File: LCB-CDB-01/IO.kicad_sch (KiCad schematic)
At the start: 64 parts, among them J100 Conn_01x02, J101 Conn_01x02, J102 Conn_01x02, J103 Conn_01x02, J104 Conn_01x02, J105 Conn_01x02, J106 Conn_01x02, J107 Conn_01x02, J130 Conn_01x02, J131 Conn_01x02, J132 Conn_01x02, J133 Conn_01x02, J134 Conn_01x02, J135 Conn_01x02, J136 Conn_01x02, J137 Conn_01x02, J138 Conn_01x02, J139 Conn_01x02, J140 Conn_01x02, J141 Conn_01x02, J150 Conn_01x02, J151 Conn_01x02, J152 Conn_01x02, J153 Conn_01x02, J154 Conn_01x02, J155 Conn_01x02, J156 Conn_01x02, J157 Conn_01x02, J158 Conn_01x02, J159 Conn_01x02, J160 Conn_01x02, J161 Conn_01x02, SW1 SW_Push, SW2 SW_Push, SW3 SW_Push, SW4 SW_Push, U100 ST_6CH_CMOS_SOIC14_MC74HC14ADG, U101 ST_6CH_CMOS_SOIC14_MC74HC14ADG

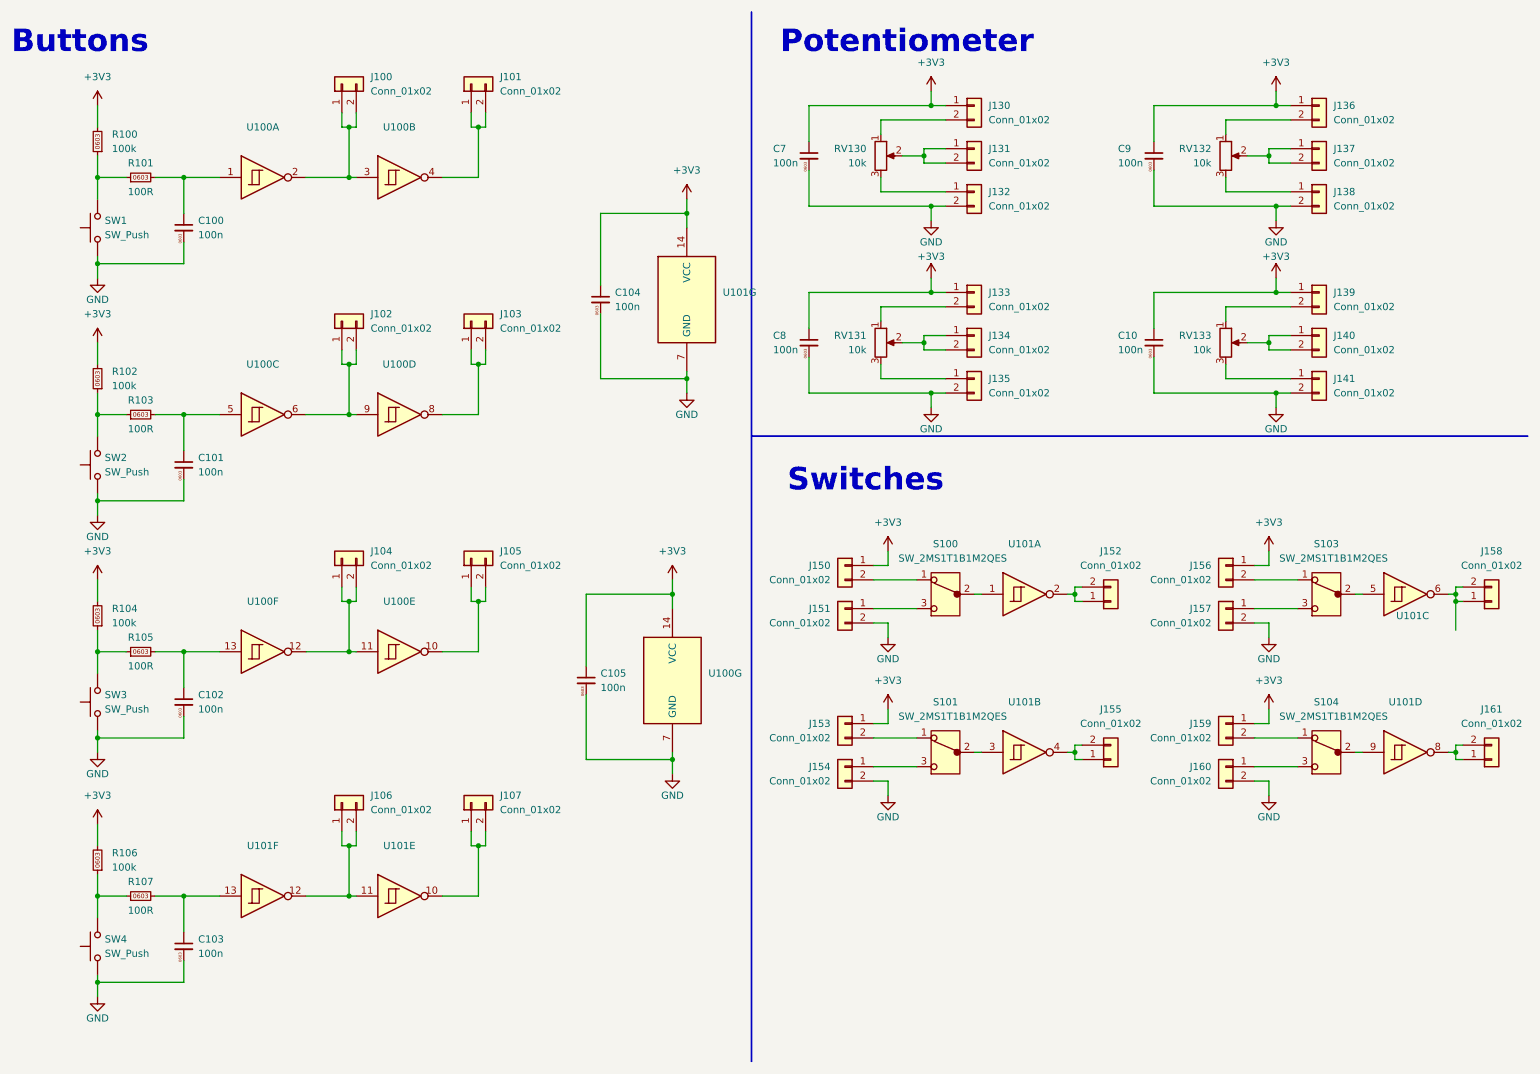
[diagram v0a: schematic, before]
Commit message: update some Rs and Cs names and values, as they can be separate values in KiCad7
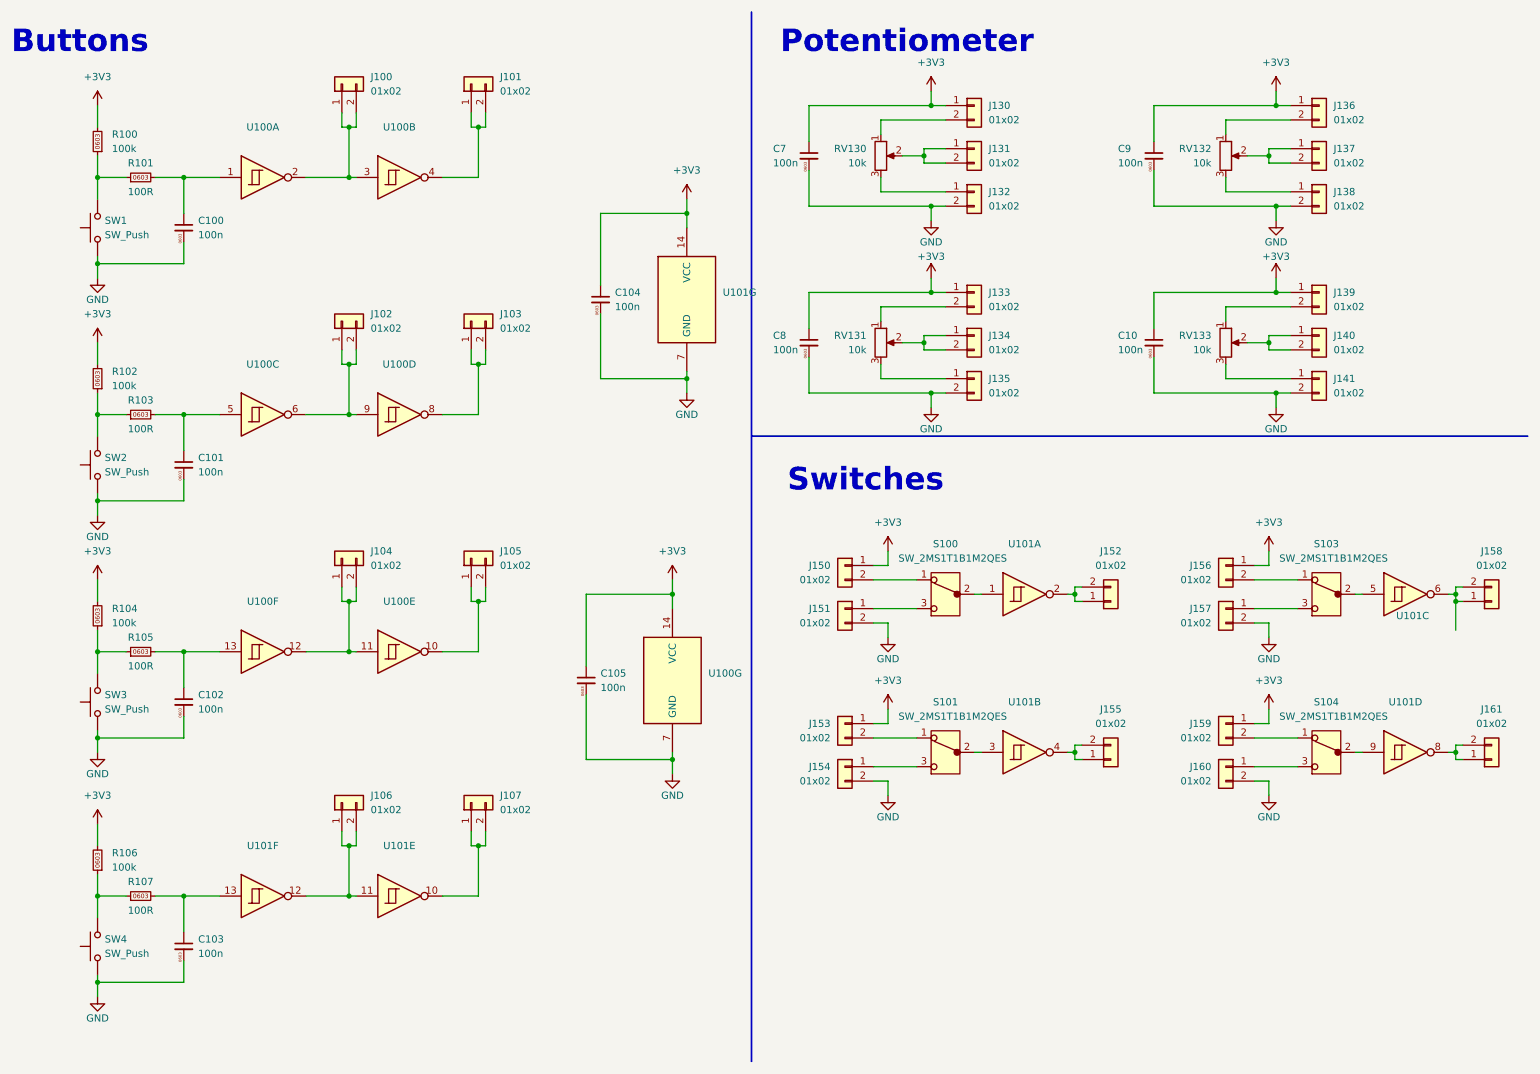
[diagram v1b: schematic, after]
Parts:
- J100, J101, J102, J103, J104, J105, J106, J107, J130, J131, J132, J133, J134, J135, J136, J137, J138, J139, J140, J141, J150, J151, J152, J153, J154, J155, J156, J157, J158, J159, J160, J161: value Conn_01x02 -> 01x02
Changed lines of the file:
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@@
       (effects (font (size 1.27 1.27)) (justify left))
     )
-    (property "Value" "Conn_01x02" (at 189.23 31.7499 0)
+    (property "Value" "01x02" (at 189.23 31.7499 0)
       (effects (font (size 1.27 1.27)) (justify left))
     )
@@
       (effects (font (size 1.27 1.27)) (justify left))
     )
-    (property "Value" "Conn_01x02" (at 161.29 148.5899 0)
+    (property "Value" "01x02" (at 161.29 148.5899 0)
       (effects (font (size 1.27 1.27)) (justify left))
     )
@@
       (effects (font (size 1.27 1.27)) (justify left))
     )
-    (property "Value" "Conn_01x02" (at 228.6 120.6499 0)
+    (property "Value" "01x02" (at 228.6 120.6499 0)
       (effects (font (size 1.27 1.27)) (justify left))
     )
@@
       (effects (font (size 1.27 1.27)) (justify left))
     )
-    (property "Value" "Conn_01x02" (at 189.23 72.3899 0)
+    (property "Value" "01x02" (at 189.23 72.3899 0)
       (effects (font (size 1.27 1.27)) (justify left))
     )
@@
       (effects (font (size 1.27 1.27)) (justify left))
     )
-    (property "Value" "Conn_01x02" (at 250.19 39.3699 0)
+    (property "Value" "01x02" (at 250.19 39.3699 0)
       (effects (font (size 1.27 1.27)) (justify left))
     )
@@
       (effects (font (size 1.27 1.27)) (justify left))
     )
-    (property "Value" "Conn_01x02" (at 161.29 140.9699 0)
+    (property "Value" "01x02" (at 161.29 140.9699 0)
       (effects (font (size 1.27 1.27)) (justify left))
     )
@@
       (effects (font (size 1.27 1.27)) (justify left))
     )
-    (property "Value" "Conn_01x02" (at 250.19 80.0099 0)
+    (property "Value" "01x02" (at 250.19 80.0099 0)
       (effects (font (size 1.27 1.27)) (justify left))
     )
@@
       (effects (font (size 1.27 1.27)) (justify left))
     )
-    (property "Value" "Conn_01x02" (at 189.23 80.0099 0)
+    (property "Value" "01x02" (at 189.23 80.0099 0)
       (effects (font (size 1.27 1.27)) (justify left))
     )
@@
       (effects (font (size 1.27 1.27)) (justify right))
     )
-    (property "Value" "Conn_01x02" (at 80.01 68.5799 90)
+    (property "Value" "01x02" (at 80.01 68.5799 90)
       (effects (font (size 1.27 1.27)) (justify right))
     )
@@
       (effects (font (size 1.27 1.27)) (justify left))
     )
-    (property "Value" "Conn_01x02" (at 189.23 39.3699 0)
+    (property "Value" "01x02" (at 189.23 39.3699 0)
       (effects (font (size 1.27 1.27)) (justify left))
     )
@@
       (effects (font (size 1.27 1.27)))
     )
-    (property "Value" "Conn_01x02" (at 210.82 138.43 0)
+    (property "Value" "01x02" (at 210.82 138.43 0)
       (effects (font (size 1.27 1.27)))
     )
@@
       (effects (font (size 1.27 1.27)) (justify right))
     )
-    (property "Value" "Conn_01x02" (at 80.01 153.6699 90)
+    (property "Value" "01x02" (at 80.01 153.6699 90)
       (effects (font (size 1.27 1.27)) (justify right))
     )
@@
       (effects (font (size 1.27 1.27)) (justify left))
     )
-    (property "Value" "Conn_01x02" (at 189.23 46.9899 0)
+    (property "Value" "01x02" (at 189.23 46.9899 0)
       (effects (font (size 1.27 1.27)) (justify left))
     )
@@
       (effects (font (size 1.27 1.27)) (justify left))
     )
-    (property "Value" "Conn_01x02" (at 189.23 64.7699 0)
+    (property "Value" "01x02" (at 189.23 64.7699 0)
       (effects (font (size 1.27 1.27)) (justify left))
     )
@@
       (effects (font (size 1.27 1.27)) (justify left))
     )
-    (property "Value" "Conn_01x02" (at 161.29 120.6499 0)
+    (property "Value" "01x02" (at 161.29 120.6499 0)
       (effects (font (size 1.27 1.27)) (justify left))
     )
@@
       (effects (font (size 1.27 1.27)) (justify right))
     )
-    (property "Value" "Conn_01x02" (at 102.87 26.6699 90)
+    (property "Value" "01x02" (at 102.87 26.6699 90)
       (effects (font (size 1.27 1.27)) (justify right))
     )
@@
       (effects (font (size 1.27 1.27)) (justify left))
     )
-    (property "Value" "Conn_01x02" (at 250.19 64.7699 0)
+    (property "Value" "01x02" (at 250.19 64.7699 0)
       (effects (font (size 1.27 1.27)) (justify left))
     )
@@
       (effects (font (size 1.27 1.27)) (justify left))
     )
-    (property "Value" "Conn_01x02" (at 228.6 113.0299 0)
+    (property "Value" "01x02" (at 228.6 113.0299 0)
       (effects (font (size 1.27 1.27)) (justify left))
     )
@@
       (effects (font (size 1.27 1.27)) (justify left))
     )
-    (property "Value" "Conn_01x02" (at 228.6 140.9699 0)
+    (property "Value" "01x02" (at 228.6 140.9699 0)
       (effects (font (size 1.27 1.27)) (justify left))
     )
@@
       (effects (font (size 1.27 1.27)) (justify right))
     )
-    (property "Value" "Conn_01x02" (at 102.87 153.6699 90)
+    (property "Value" "01x02" (at 102.87 153.6699 90)
       (effects (font (size 1.27 1.27)) (justify right))
     )
@@
       (effects (font (size 1.27 1.27)) (justify right))
     )
-    (property "Value" "Conn_01x02" (at 80.01 26.6699 90)
+    (property "Value" "01x02" (at 80.01 26.6699 90)
       (effects (font (size 1.27 1.27)) (justify right))
     )
@@
       (effects (font (size 1.27 1.27)) (justify right))
     )
-    (property "Value" "Conn_01x02" (at 102.87 110.4899 90)
+    (property "Value" "01x02" (at 102.87 110.4899 90)
       (effects (font (size 1.27 1.27)) (justify right))
     )
@@
       (effects (font (size 1.27 1.27)))
     )
-    (property "Value" "Conn_01x02" (at 278.13 110.49 0)
+    (property "Value" "01x02" (at 278.13 110.49 0)
       (effects (font (size 1.27 1.27)))
     )
@@
       (effects (font (size 1.27 1.27)) (justify left))
     )
-    (property "Value" "Conn_01x02" (at 161.29 113.0299 0)
+    (property "Value" "01x02" (at 161.29 113.0299 0)
       (effects (font (size 1.27 1.27)) (justify left))
     )
@@
       (effects (font (size 1.27 1.27)) (justify left))
     )
-    (property "Value" "Conn_01x02" (at 250.19 72.3899 0)
+    (property "Value" "01x02" (at 250.19 72.3899 0)
       (effects (font (size 1.27 1.27)) (justify left))
     )
@@
       (effects (font (size 1.27 1.27)) (justify left))
     )
-    (property "Value" "Conn_01x02" (at 228.6 148.5899 0)
+    (property "Value" "01x02" (at 228.6 148.5899 0)
       (effects (font (size 1.27 1.27)) (justify left))
     )
@@
       (effects (font (size 1.27 1.27)) (justify left))
     )
-    (property "Value" "Conn_01x02" (at 250.19 46.9899 0)
+    (property "Value" "01x02" (at 250.19 46.9899 0)
       (effects (font (size 1.27 1.27)) (justify left))
     )
@@
       (effects (font (size 1.27 1.27)) (justify right))
     )
-    (property "Value" "Conn_01x02" (at 80.01 110.4899 90)
+    (property "Value" "01x02" (at 80.01 110.4899 90)
       (effects (font (size 1.27 1.27)) (justify right))
     )
@@
       (effects (font (size 1.27 1.27)) (justify right))
     )
-    (property "Value" "Conn_01x02" (at 102.87 68.5799 90)
+    (property "Value" "01x02" (at 102.87 68.5799 90)
       (effects (font (size 1.27 1.27)) (justify right))
     )
@@
       (effects (font (size 1.27 1.27)) (justify left))
     )
-    (property "Value" "Conn_01x02" (at 250.19 31.7499 0)
+    (property "Value" "01x02" (at 250.19 31.7499 0)
       (effects (font (size 1.27 1.27)) (justify left))
     )
@@
       (effects (font (size 1.27 1.27)))
     )
-    (property "Value" "Conn_01x02" (at 210.82 110.49 0)
+    (property "Value" "01x02" (at 210.82 110.49 0)
       (effects (font (size 1.27 1.27)))
     )
@@
       (effects (font (size 1.27 1.27)))
     )
-    (property "Value" "Conn_01x02" (at 278.13 138.43 0)
+    (property "Value" "01x02" (at 278.13 138.43 0)
       (effects (font (size 1.27 1.27)))
     )

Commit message: bump version to 1.1.0
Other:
- title: LCB-CBD-001: Dock -> LCB-CBD-01: Dock
- moved on the sheet: C104, U101G
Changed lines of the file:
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@@
   (paper "A4")
   (title_block
-    (title "LCB-CBD-001: Dock")
-    (date "2022-08-12")
-    (rev "0.1")
+    (title "LCB-CBD-01: Dock")
+    (date "2023-04-13")
+    (rev "1.1.0")
     (company "PADERBORN UNIVERSITY DEPARTMENT OF POWER ELECTRONICS AND ELECTRICAL DRIVES")
   )
@@
   (junction (at 76.2 116.84) (diameter 0) (color 0 0 0 0)
   )
-  (junction (at 271.78 116.84) (diameter 0) (color 0 0 0 0)
-  )
-  (junction (at 135.89 48.26) (diameter 0) (color 0 0 0 0)
+  (junction (at 132.08 48.26) (diameter 0) (color 0 0 0 0)
   )
   (junction (at 238.76 71.12) (diameter 0) (color 0 0 0 0)
@@
   (junction (at 31.75 99.06) (diameter 0) (color 0 0 0 0)
   )
-  (junction (at 135.89 77.47) (diameter 0) (color 0 0 0 0)
+  (junction (at 132.08 77.47) (diameter 0) (color 0 0 0 0)
   )
   (junction (at 240.03 46.99) (diameter 0) (color 0 0 0 0)
@@
     (stroke (width 0) (type default))
   )
-  (wire (pts (xy 135.89 77.47) (xy 120.65 77.47))
+  (wire (pts (xy 132.08 77.47) (xy 116.84 77.47))
     (stroke (width 0) (type default))
   )
@@
     (stroke (width 0) (type default))
   )
-  (wire (pts (xy 135.89 77.47) (xy 135.89 80.01))
+  (wire (pts (xy 132.08 77.47) (xy 132.08 80.01))
     (stroke (width 0) (type default))
   )
@@
     (stroke (width 0) (type default))
   )
-  (wire (pts (xy 271.78 121.92) (xy 271.78 116.84))
-    (stroke (width 0) (type default))
-  )
   (wire (pts (xy 231.14 64.77) (xy 242.57 64.77))
     (stroke (width 0) (type default))
@@
     (stroke (width 0) (type default))
   )
-  (wire (pts (xy 120.65 48.26) (xy 120.65 60.96))
+  (wire (pts (xy 116.84 48.26) (xy 116.84 60.96))
     (stroke (width 0) (type default))
   )
@@
     (stroke (width 0) (type default))
   )
-  (wire (pts (xy 135.89 76.2) (xy 135.89 77.47))
+  (wire (pts (xy 132.08 76.2) (xy 132.08 77.47))
     (stroke (width 0) (type default))
   )
@@
     (stroke (width 0) (type default))
   )
-  (wire (pts (xy 120.65 77.47) (xy 120.65 66.04))
+  (wire (pts (xy 116.84 77.47) (xy 116.84 66.04))
     (stroke (width 0) (type default))
   )
@@
     (stroke (width 0) (type default))
   )
-  (wire (pts (xy 135.89 48.26) (xy 120.65 48.26))
+  (wire (pts (xy 132.08 48.26) (xy 116.84 48.26))
     (stroke (width 0) (type default))
   )
@@
     (stroke (width 0) (type default))
   )
-  (wire (pts (xy 135.89 48.26) (xy 135.89 50.8))
+  (wire (pts (xy 132.08 48.26) (xy 132.08 50.8))
     (stroke (width 0) (type default))
   )
@@
     (stroke (width 0) (type default))
   )
-  (wire (pts (xy 135.89 45.72) (xy 135.89 48.26))
+  (wire (pts (xy 132.08 45.72) (xy 132.08 48.26))
     (stroke (width 0) (type default))
   )
@@
     )
   )
-  (symbol (lib_id "LEA_SymbolLibrary:C_0603_100n_X5R_10P__50V") (at 120.65 63.5 0) (unit 1)
+  (symbol (lib_id "LEA_SymbolLibrary:C_0603_100n_X5R_10P__50V") (at 116.84 63.5 0) (unit 1)
     (in_bom yes) (on_board yes) (dnp no) (fields_autoplaced)
-    (property "Reference" "C104" (at 123.19 62.2362 0)
+    (property "Reference" "C104" (at 119.38 62.2362 0)
       (effects (font (size 1.27 1.27)) (justify left))
     )
-    (property "Value" "100n" (at 123.19 64.7762 0)
+    (property "Value" "100n" (at 119.38 64.7762 0)
       (effects (font (size 1.27 1.27)) (justify left))
     )
-    (property "Footprint" "LEA_FootprintLibrary:C_0603" (at 120.65 53.34 0)
+    (property "Footprint" "LEA_FootprintLibrary:C_0603" (at 116.84 53.34 0)
       (effects (font (size 1.27 1.27)) hide)
     )
-    (property "Datasheet" "" (at 120.65 63.5 0)
+    (property "Datasheet" "" (at 116.84 63.5 0)
       (effects (font (size 1.27 1.27)) hide)
     )
-    (property "Mfr. No" "" (at 120.65 63.5 0)
+    (property "Mfr. No" "" (at 116.84 63.5 0)
       (effects (font (size 1.27 1.27)) hide)
     )
-    (property "Manufacturer" "TDK" (at 120.65 63.5 0)
+    (property "Manufacturer" "TDK" (at 116.84 63.5 0)
       (effects (font (size 1.27 1.27)) hide)
     )
-    (property "Mouser No" "" (at 120.65 63.5 0)
+    (property "Mouser No" "" (at 116.84 63.5 0)
       (effects (font (size 1.27 1.27)) hide)
     )
-    (property "manf#" "C1608X5R1H104K" (at 120.65 63.5 0)
+    (property "manf#" "C1608X5R1H104K" (at 116.84 63.5 0)
       (effects (font (size 1.27 1.27)) hide)
     )
-    (property "mouser#" "810-C1608X5R1H104K" (at 120.65 63.5 0)
+    (property "mouser#" "810-C1608X5R1H104K" (at 116.84 63.5 0)
       (effects (font (size 1.27 1.27)) hide)
     )
@@
     )
   )
-  (symbol (lib_id "LEA_SymbolLibrary:GND") (at 135.89 80.01 0) (unit 1)
+  (symbol (lib_id "LEA_SymbolLibrary:GND") (at 132.08 80.01 0) (unit 1)
     (in_bom yes) (on_board yes) (dnp no)
-    (property "Reference" "#PWR014" (at 138.43 82.55 90)
+    (property "Reference" "#PWR014" (at 134.62 82.55 90)
       (effects (font (size 1.27 1.27)) hide)
     )
-    (property "Value" "GND" (at 135.89 83.82 0)
+    (property "Value" "GND" (at 132.08 83.82 0)
       (effects (font (size 1.27 1.27)))
     )
-    (property "Footprint" "" (at 135.89 80.01 0)
+    (property "Footprint" "" (at 132.08 80.01 0)
       (effects (font (size 1.27 1.27)) hide)
     )
-    (property "Datasheet" "" (at 135.89 80.01 0)
+    (property "Datasheet" "" (at 132.08 80.01 0)
       (effects (font (size 1.27 1.27)) hide)
     )
@@
     )
   )
-  (symbol (lib_id "LEA_SymbolLibrary:ST_6CH_CMOS_SOIC14_MC74HC14ADG") (at 135.89 63.5 0) (unit 7)
+  (symbol (lib_id "LEA_SymbolLibrary:ST_6CH_CMOS_SOIC14_MC74HC14ADG") (at 132.08 63.5 0) (unit 7)
     (in_bom yes) (on_board yes) (dnp no) (fields_autoplaced)
-    (property "Reference" "U101" (at 142.24 62.2299 0)
+    (property "Reference" "U101" (at 138.43 62.2299 0)
       (effects (font (size 1.27 1.27)) (justify left))
     )
-    (property "Value" "ST_6CH_CMOS_SOIC14_MC74HC14ADG" (at 135.89 64.77 0)
+    (property "Value" "ST_6CH_CMOS_SOIC14_MC74HC14ADG" (at 132.08 64.77 0)
       (effects (font (size 1.27 1.27)) hide)
     )
-    (property "Footprint" "LEA_FootprintLibrary:SOIC-14" (at 134.62 52.07 0)
+    (property "Footprint" "LEA_FootprintLibrary:SOIC-14" (at 130.81 52.07 0)
       (effects (font (size 1.27 1.27)) hide)
     )
-    (property "Datasheet" "https://www.mouser.de/datasheet/2/308/1/MC74HC14A_D-2315678.pdf" (at 135.89 55.88 0)
+    (property "Datasheet" "https://www.mouser.de/datasheet/2/308/1/MC74HC14A_D-2315678.pdf" (at 132.08 55.88 0)
       (effects (font (size 1.27 1.27)) hide)
     )
-    (property "Manufacturer" "Onsemi" (at 125.73 46.99 0)
+    (property "Manufacturer" "Onsemi" (at 121.92 46.99 0)
       (effects (font (size 1.27 1.27)) hide)
     )
-    (property "Mouser No." "863-MC74HC14ADG " (at 132.08 49.53 0)
+    (property "Mouser No." "863-MC74HC14ADG " (at 128.27 49.53 0)
       (effects (font (size 1.27 1.27)) hide)
     )
-    (property "mouser#" "863-MC74HC14ADG " (at 132.08 49.53 0)
+    (property "mouser#" "863-MC74HC14ADG " (at 128.27 49.53 0)
       (effects (font (size 1.27 1.27)) hide)
     )
-    (property "manf#" "MC74HC14ADG " (at 132.08 58.42 0)
+    (property "manf#" "MC74HC14ADG " (at 128.27 58.42 0)
       (effects (font (size 1.27 1.27)) hide)
     )
@@
     )
   )
-  (symbol (lib_id "LEA_SymbolLibrary:+3V3") (at 135.89 45.72 0) (unit 1)
+  (symbol (lib_id "LEA_SymbolLibrary:+3V3") (at 132.08 45.72 0) (unit 1)
     (in_bom yes) (on_board yes) (dnp no) (fields_autoplaced)
-    (property "Reference" "#PWR013" (at 137.16 45.72 90)
+    (property "Reference" "#PWR013" (at 133.35 45.72 90)
       (effects (font (size 1.27 1.27)) hide)
     )
-    (property "Value" "+3V3" (at 135.89 40.64 0)
+    (property "Value" "+3V3" (at 132.08 40.64 0)
       (effects (font (size 1.27 1.27)))
     )
-    (property "Footprint" "" (at 135.89 45.72 0)
+    (property "Footprint" "" (at 132.08 45.72 0)
       (effects (font (size 1.27 1.27)) hide)
     )
-    (property "Datasheet" "" (at 135.89 45.72 0)
+    (property "Datasheet" "" (at 132.08 45.72 0)
       (effects (font (size 1.27 1.27)) hide)
     )
